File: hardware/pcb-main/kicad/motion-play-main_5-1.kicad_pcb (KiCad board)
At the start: 4 copper layers, 86.4 x 35 mm, 37 parts, among them IC1 SN74AHCT125PWR, J2 DWEII Power Module, J3 LED_Strip, J4 Conn_01x05, J5 Conn_01x05, J6 Conn_01x05, U1 AP2112K-3.3TRG1, U2 T-Display-S3, U4 TCA9548APWR

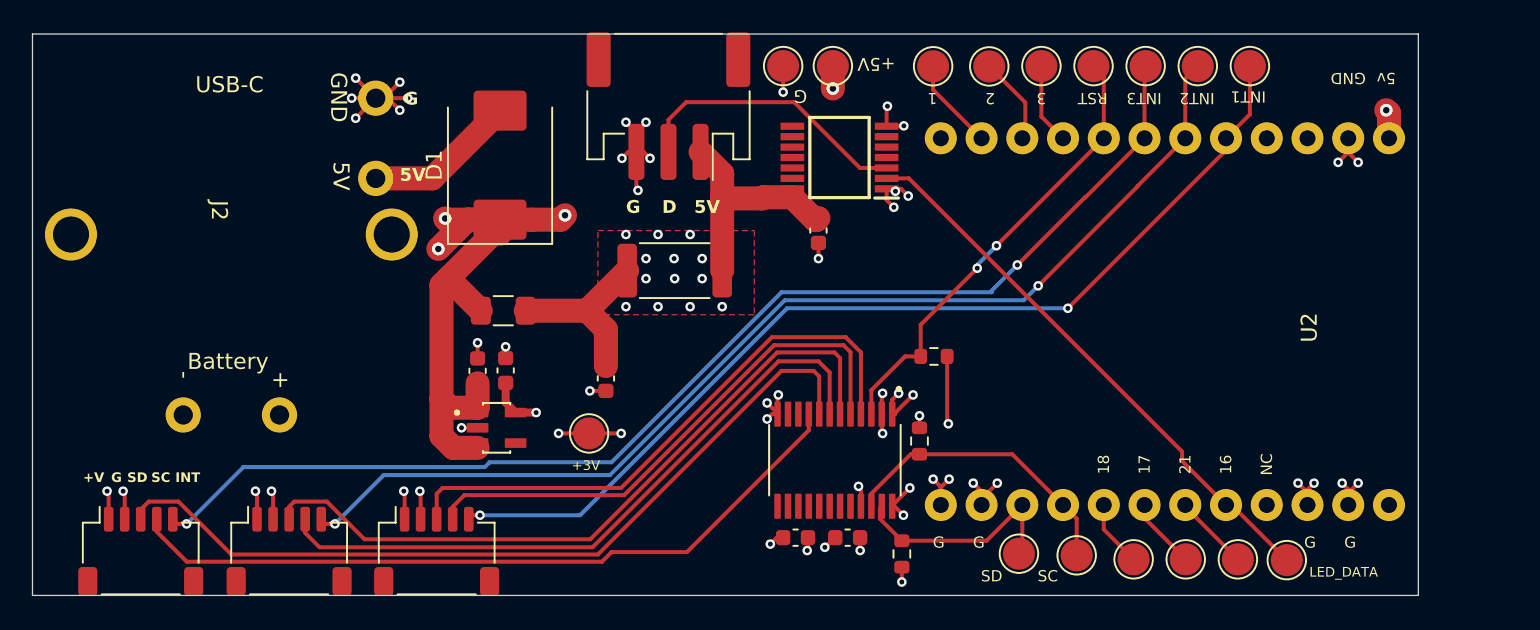
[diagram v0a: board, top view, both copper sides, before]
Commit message: Proximity detection and updated pcbs
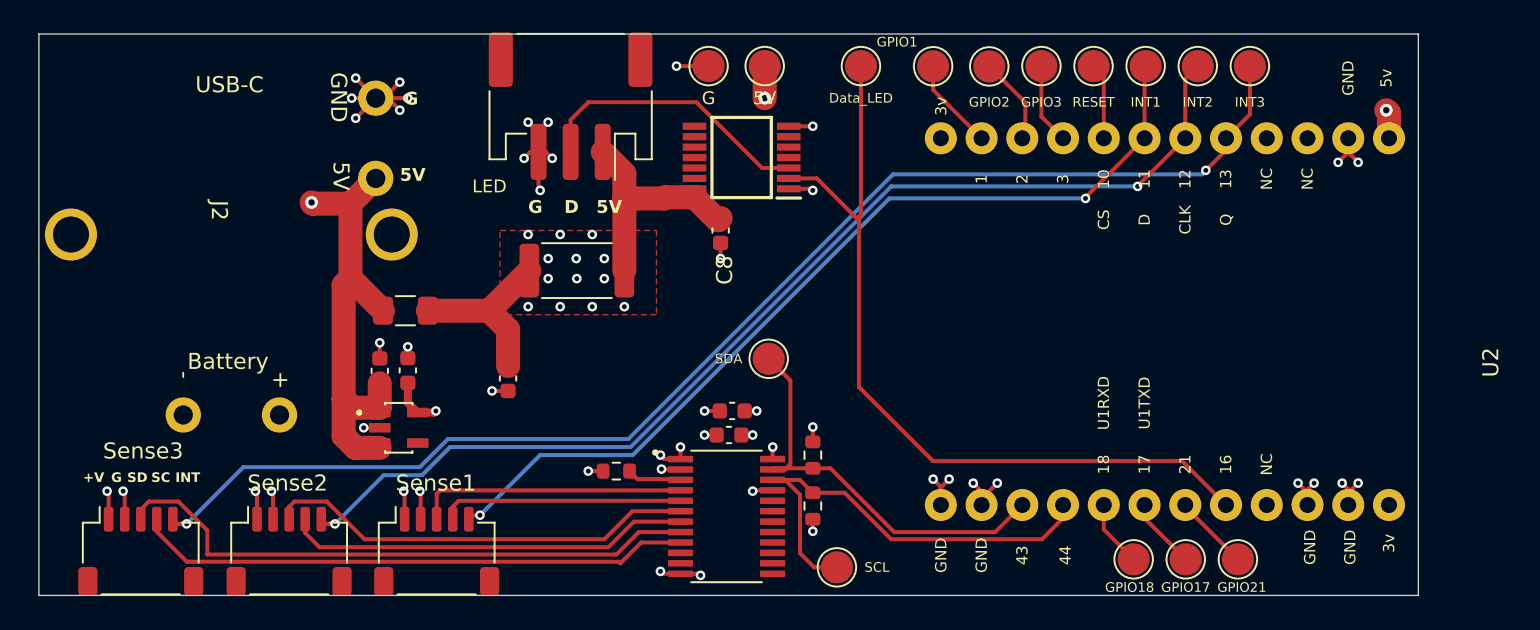
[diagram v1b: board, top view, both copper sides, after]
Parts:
- removed D1: D_Schottky, Diode_SMD:D_SMC
- removed TP_3V1: TestPoint, TestPoint:TestPoint_Pad_D2.0mm
- moved TPIO16 40.7 mm to (129.2, 103.0)
- moved R6 21.1 mm to (114.0, 128.2), turned to 180 degrees
- moved TPIO43 19.8 mm to (123.5, 121.2)
- moved TPIO44 15.0 mm to (127.8, 134.2)
- moved C9 9.78 mm to (121.0, 126.0)
- moved C10 8.83 mm to (121.2, 124.5)
- moved R28 8.29 mm to (126.2, 127.2), turned to 90 degrees
- moved R29 7.79 mm to (126.2, 130.4), turned to -90 degrees
- moved U4 7.61 mm to (120.9, 131.1), turned to 0 degrees
- moved F1 6.10 mm to (100.8, 118.2)
- moved IC1 6.10 mm to (121.8, 108.7)
- moved R27 6.10 mm to (111.5, 115.8)
- moved C1 6.10 mm to (99.2, 122.0)
- moved C2 6.10 mm to (101.0, 122.0)
- moved C7 6.10 mm to (107.2, 122.5)
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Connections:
- J2 pad 2: Net-(D1-A) -> +5V
- TPIO11 pad 1: /INT3 -> /INT1
- TPIO13 pad 1: /INT1 -> /INT3
- U2 pad 6: /INT3 -> /INT1
- U2 pad 8: /INT1 -> /INT3
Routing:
- net /TCA9548A_Subsystem/TCA_RESET: track 28.7 -> 8.37 mm, vias 2 -> 0
- net /TCA9548A_Subsystem/CH0_SDA: track 36.3 -> 16.9 mm
- net /TCA9548A_Subsystem/CH0_SCL: track 33.8 -> 15.1 mm
- net /TCA9548A_Subsystem/CH1_SDA: track 44.7 -> 27.0 mm
- net /TCA9548A_Subsystem/CH1_SCL: track 41.6 -> 25.3 mm
- net /LED Controller/DATA_IN: track 35.2 -> 51.5 mm
- net /TCA9548A_Subsystem/CH2_SDA: track 51.7 -> 37.3 mm
- net /I2C_SDA: track 14.8 -> 26.7 mm
- net /TCA9548A_Subsystem/CH2_SCL: track 46.6 -> 34.8 mm
- net /I2C_SCL: track 19.4 -> 29.4 mm
- net Net-(D1-A): track 9.50 -> 0.00 mm
- net +3.3V: track 22.7 -> 13.4 mm, vias 13 -> 10
- net +5V: track 42.3 -> 34.6 mm, vias 5 -> 3
- net GND: track 66.3 -> 60.2 mm, vias 58 -> 53
- net /INT1: track 62.6 -> 57.0 mm
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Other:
- board size 86.4 x 35 mm -> 86 x 35 mm
- board text removed: "+5V"
- board text removed: "1"
- board text removed: "LED_DATA"
